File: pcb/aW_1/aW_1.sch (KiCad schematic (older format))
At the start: 113 parts, among them J1 USB4110-GF-A, J2 USB4110-GF-A, J3 USB4110-GF-A, J4 Conn_ARM_JTAG_SWD_10, K1 KEYSW, K10 KEYSW, K11 KEYSW, K12 KEYSW, K13 KEYSW, K14 KEYSW, K15 KEYSW, K16 KEYSW, K17 KEYSW, K18 KEYSW, K19 KEYSW, K2 KEYSW, K20 KEYSW, K21 KEYSW, K22 KEYSW, K23 KEYSW, K24 KEYSW, K25 KEYSW, K26 KEYSW, K27 KEYSW, K28 KEYSW, K29 KEYSW, K3 KEYSW, K30 KEYSW, K31 KEYSW, K32 KEYSW, K33 KEYSW, K4 KEYSW, K5 KEYSW, K6 KEYSW, K7 KEYSW, K8 KEYSW, K9 KEYSW, Q1 Q_PMOS_SDG, SW1 BTN1, SW2 BTN2, U1 AP2112K-3.3TRG1, U2 MCP23017T-E_SS, U3 MCP73831-2-OT, U4 FT231XS-R, U5 BL652-SA-01-T_R, Y1 32.768

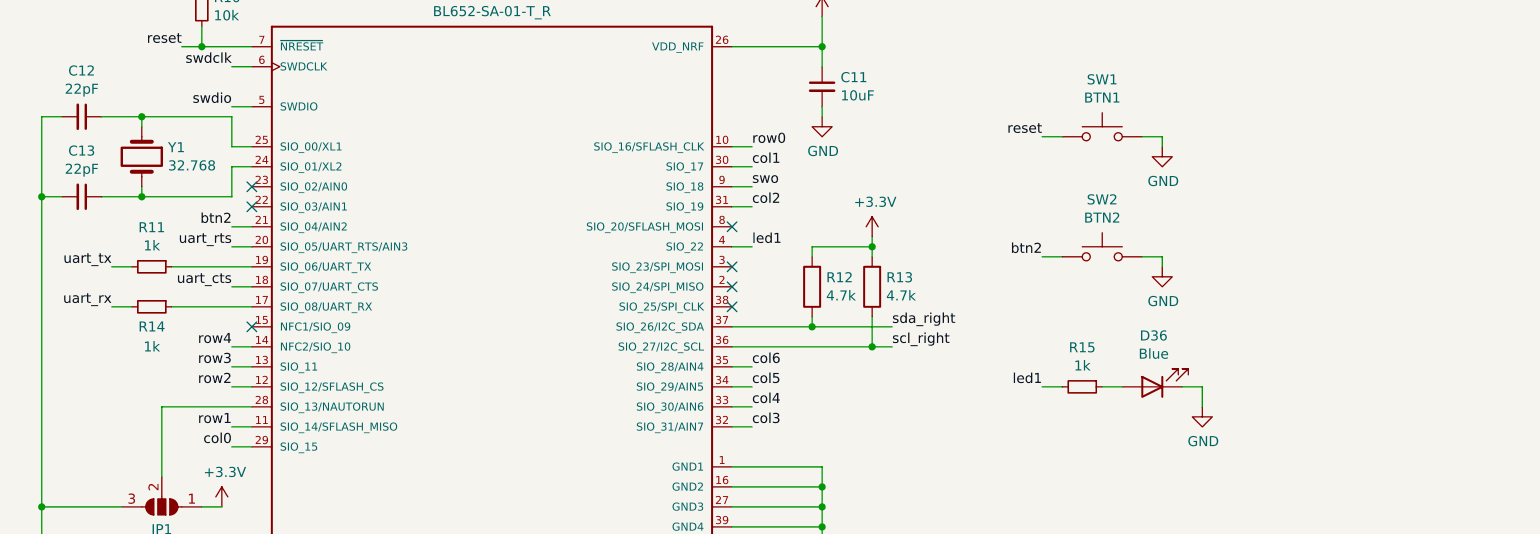
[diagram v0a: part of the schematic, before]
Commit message: Added voltage divider for battery measurement, improved gnd pour
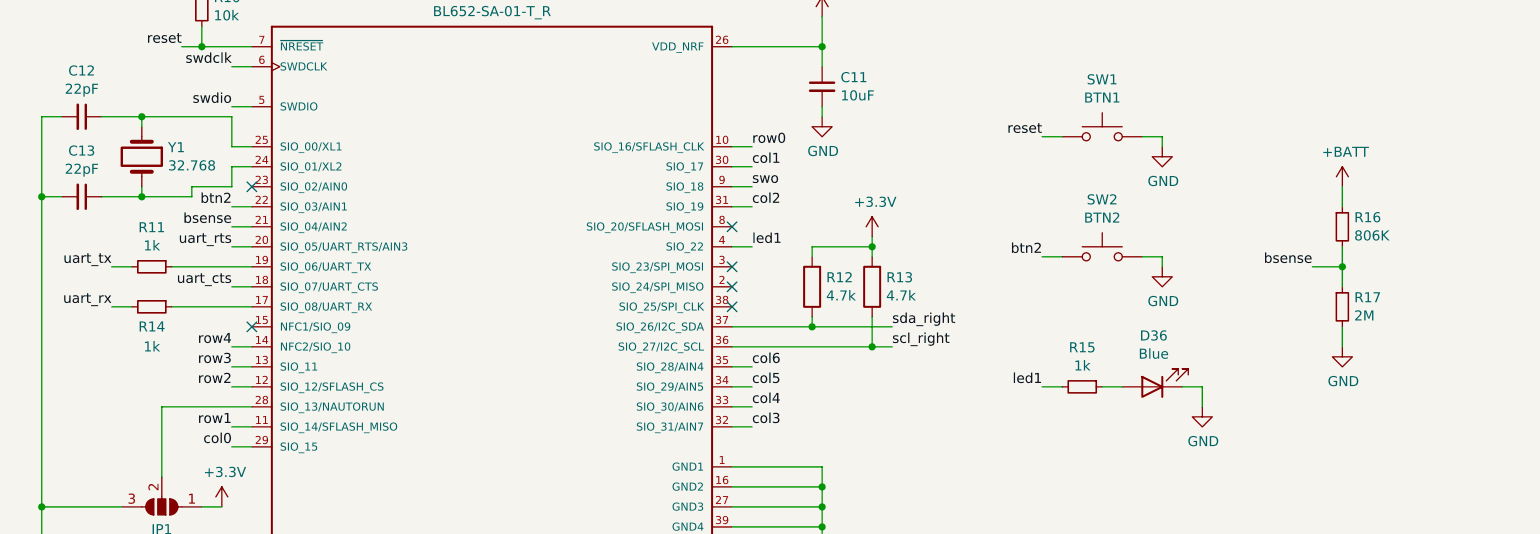
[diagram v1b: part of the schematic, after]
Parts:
- added R16: 806K, Resistor_SMD:R_0603_1608Metric, symbol Device:R_Small
- added R17: 2M, Resistor_SMD:R_0603_1608Metric, symbol Device:R_Small
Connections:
- net +BATT: now also R16.1
- net GND: now also R17.2
- net btn2: now also U5.22 (SIO_03/AIN1); no longer U5.21 (SIO_04/AIN2)
- new net bsense: R16.2, R17.1, U5.21 (SIO_04/AIN2)
- no-connect marks 34 -> 33
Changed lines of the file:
@@
 	2150 8650 2050 8650
-Wire Wire Line
-	2050 8650 2050 8800
-Wire Wire Line
-	2050 8800 1600 8800
 Wire Wire Line
 	1600 8800 1600 8750
@@
 Wire Wire Line
 	6700 8500 6700 8550
-Text Label 2050 8950 2    50   ~ 0
+Text Label 2050 8850 2    50   ~ 0
 btn2
 Wire Wire Line
@@
 NoConn ~ 2150 9450
 NoConn ~ 2150 8750
-NoConn ~ 2150 8850
 Wire Wire Line
 	9450 5700 9400 5700
@@
 	3600 1550 3600 1950
 Connection ~ 3600 1950
+$Comp
+L power:+BATT #PWR0104
+U 1 1 5F0170FA
+P 7600 8750
+F 0 "#PWR0104" H 7600 8600 50  0001 C CNN
+F 1 "+BATT" H 7615 8923 50  0000 C CNN
+F 2 "" H 7600 8750 50  0001 C CNN
+F 3 "" H 7600 8750 50  0001 C CNN
+	1    7600 8750
+	1    0    0    -1
+$EndComp
+$Comp
+L Device:R_Small R16
+U 1 1 5F018400
+P 7600 8950
+F 0 "R16" H 7659 8996 50  0000 L CNN
+F 1 "806K" H 7659 8905 50  0000 L CNN
+F 2 "Resistor_SMD:R_0603_1608Metric" H 7600 8950 50  0001 C CNN
+F 3 "~" H 7600 8950 50  0001 C CNN
+	1    7600 8950
+	1    0    0    -1
+$EndComp
+$Comp
+L Device:R_Small R17
+U 1 1 5F018BB8
+P 7600 9350
+F 0 "R17" H 7659 9396 50  0000 L CNN
+F 1 "2M" H 7659 9305 50  0000 L CNN
+F 2 "Resistor_SMD:R_0603_1608Metric" H 7600 9350 50  0001 C CNN
+F 3 "~" H 7600 9350 50  0001 C CNN
+	1    7600 9350
+	1    0    0    -1
+$EndComp
+Text Label 2050 8950 2    50   ~ 0
+bsense
+Wire Wire Line
+	2050 8850 2150 8850
+Wire Wire Line
+	2050 8750 1850 8750
+Wire Wire Line
+	1850 8750 1850 8800
+Wire Wire Line
+	2050 8650 2050 8750
+Wire Wire Line
+	1600 8800 1850 8800
+Text Label 7450 9150 2    50   ~ 0
+bsense
+$Comp
+L power:GND #PWR0105
+U 1 1 5F2C0026
+P 7600 9550
+F 0 "#PWR0105" H 7600 9300 50  0001 C CNN
+F 1 "GND" H 7605 9377 50  0000 C CNN
+F 2 "" H 7600 9550 50  0001 C CNN
+F 3 "" H 7600 9550 50  0001 C CNN
+	1    7600 9550
+	1    0    0    -1
+$EndComp
+Wire Wire Line
+	7600 8750 7600 8850
+Wire Wire Line
+	7600 9050 7600 9150
+Wire Wire Line
+	7600 9450 7600 9550
+Wire Wire Line
+	7600 9150 7450 9150
+Connection ~ 7600 9150
+Wire Wire Line
+	7600 9150 7600 9250
 $EndSCHEMATC

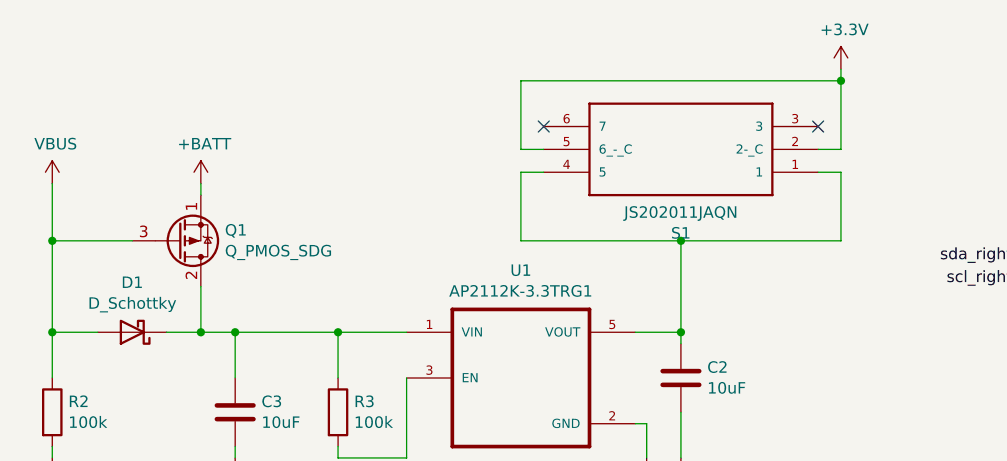
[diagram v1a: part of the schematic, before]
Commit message: Fixed mosfet and improved keepout around antenna
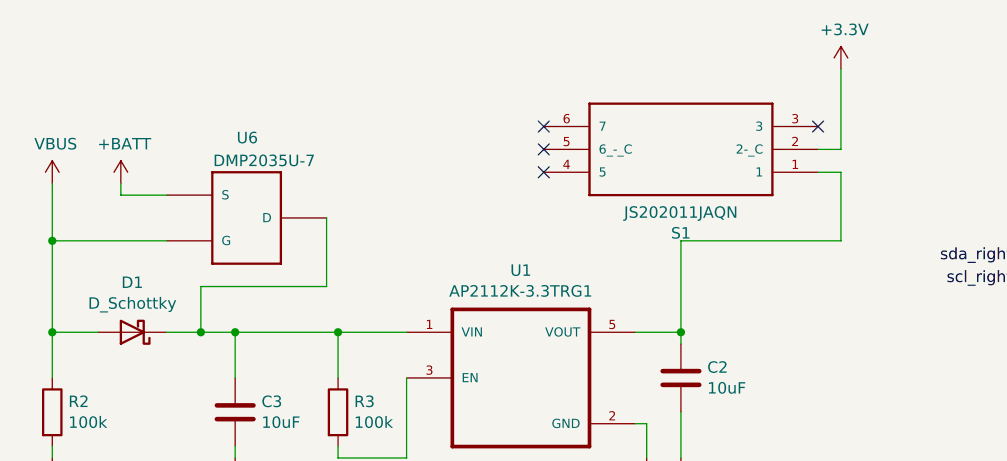
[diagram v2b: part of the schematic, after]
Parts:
- removed Q1: Q_PMOS_SDG, snap-eda:SOT23, symbol Device:Q_PMOS_SDG
- added U6: DMP2035U-7, snap-eda:SOT23, symbol SnapEDA-Library:DMP2035U-7
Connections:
- net +3V3: no longer S1.5 (6_-_C)
- net +BATT: now also U6.2 (S)
- net VBUS: now also U6.1 (G)
- net at C3.1, D1.1 (K), R3.1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: now also U6.3 (D)
- net at C2.1, S1.1, U1.5 (VOUT): no longer S1.4 (5)
- no-connect marks 33 -> 35
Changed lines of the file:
@@
 L power:+BATT #PWR03
 U 1 1 5ECBF437
-P 1500 1300
-F 0 "#PWR03" H 1500 1150 50  0001 C CNN
-F 1 "+BATT" H 1515 1473 50  0000 C CNN
-F 2 "" H 1500 1300 50  0001 C CNN
-F 3 "" H 1500 1300 50  0001 C CNN
-	1    1500 1300
+P 1150 1300
+F 0 "#PWR03" H 1150 1150 50  0001 C CNN
+F 1 "+BATT" H 1165 1473 50  0000 C CNN
+F 2 "" H 1150 1300 50  0001 C CNN
+F 3 "" H 1150 1300 50  0001 C CNN
+	1    1150 1300
 	1    0    0    -1
 $EndComp
@@
 Wire Wire Line
 	1350 1950 1500 1950
-$Comp
-L Device:Q_PMOS_SDG Q1
-U 1 1 5EDC238F
-P 1400 1550
-F 0 "Q1" H 1605 1504 50  0000 L CNN
-F 1 "Q_PMOS_SDG" H 1605 1595 50  0000 L CNN
-F 2 "snap-eda:SOT23" H 1600 1650 50  0001 C CNN
-F 3 "~" H 1400 1550 50  0001 C CNN
-	1    1400 1550
-	1    0    0    1
-$EndComp
-Wire Wire Line
-	850  1300 850  1550
-Wire Wire Line
-	850  1550 1200 1550
-Connection ~ 850  1550
-Wire Wire Line
-	850  1550 850  1950
 Wire Wire Line
 	1500 1750 1500 1950
@@
 Wire Wire Line
 	1500 1950 1650 1950
-Wire Wire Line
-	1500 1350 1500 1300
 $Comp
 L Device:C_Small C7
@@
 	-1   0    0    1
 $EndComp
-Connection ~ 3600 1550
 Wire Wire Line
 	4200 1150 4300 1150
-Wire Wire Line
-	4300 1150 4300 850
-Wire Wire Line
-	3000 1150 2900 1150
-Wire Wire Line
-	2900 1150 2900 850
-Wire Wire Line
-	2900 850  4300 850
-Connection ~ 4300 850
-Wire Wire Line
-	4300 850  4300 800
-Wire Wire Line
-	3000 1250 2900 1250
-Wire Wire Line
-	2900 1250 2900 1550
-Wire Wire Line
-	2900 1550 3600 1550
-Wire Wire Line
-	4300 1550 4300 1250
-Wire Wire Line
-	4300 1250 4200 1250
 Wire Wire Line
 	3600 1550 4300 1550
@@
 Wire Wire Line
 	7600 9150 7600 9250
+$Comp
+L SnapEDA-Library:DMP2035U-7 U6
+U 1 1 5F03DD47
+P 1550 1250
+F 0 "U6" H 1750 1100 50  0000 R CNN
+F 1 "DMP2035U-7" H 2000 1200 50  0000 R CNN
+F 2 "snap-eda:SOT23" H 1550 1250 50  0001 L BNN
+F 3 "" H 1550 1250 50  0001 C CNN
+	1    1550 1250
+	1    0    0    1
+$EndComp
+Wire Wire Line
+	850  1300 850  1550
+Wire Wire Line
+	1150 1300 1150 1350
+Wire Wire Line
+	1150 1350 1350 1350
+Wire Wire Line
+	850  1550 1350 1550
+Connection ~ 850  1550
+Wire Wire Line
+	850  1550 850  1950
+Wire Wire Line
+	2050 1450 2050 1750
+Wire Wire Line
+	2050 1750 1500 1750
+Wire Wire Line
+	4300 1250 4200 1250
+Wire Wire Line
+	4300 1550 4300 1250
+Wire Wire Line
+	4300 800  4300 1150
+NoConn ~ 3000 1150
+NoConn ~ 3000 1250
 $EndSCHEMATC
